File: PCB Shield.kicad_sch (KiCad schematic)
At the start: 48 parts, among them J1 Conn_20to49, J10 TB002-500-02BE, J11 Conn_1to20, J12 TB002-500-02BE, J13 TB002-500-02BE, J14 TB002-500-02BE, J15 TB002-500-02BE, J16 TB002-500-02BE, J17 TB002-500-02BE, J18 TB002-500-02BE, J2 Conn_01x08_Socket, J3 Conn_20to49, J6 Conn_01x04_Socket, J7 Conn_01x04_Socket, J8 Conn_1to20, J9 OSTT7020150, Q1 IRLML2502TRPBF, SW1 C1353VQNAA, U2 74AHCT125S14-13, U3 ESDA6V1L

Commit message: final saves
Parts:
- J1, J3: footprint Connector_PinHeader_2.54mm:PinHeader_1x20_P2.54mm_Vertical -> 196_Project_Footprints:196_Conn_20to48
- J11, J8: footprint Connector_PinHeader_2.54mm:PinHeader_1x20_P2.54mm_Vertical -> 196_Project_Footprints:196_Conn_1to20
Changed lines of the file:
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@@
 			)
 		)
-		(property "Footprint" "Connector_PinHeader_2.54mm:PinHeader_1x20_P2.54mm_Vertical"
+		(property "Footprint" "196_Project_Footprints:196_Conn_1to20"
 			(at 115.57 49.53 0)
 			(hide yes)
@@
 			)
 		)
-		(property "Footprint" "Connector_PinHeader_2.54mm:PinHeader_1x20_P2.54mm_Vertical"
+		(property "Footprint" "196_Project_Footprints:196_Conn_20to48"
 			(at 131.318 22.86 0)
 			(hide yes)
@@
 			)
 		)
-		(property "Footprint" "Connector_PinHeader_2.54mm:PinHeader_1x20_P2.54mm_Vertical"
+		(property "Footprint" "196_Project_Footprints:196_Conn_20to48"
 			(at 122.428 22.86 0)
 			(hide yes)
@@
 			)
 		)
-		(property "Footprint" "Connector_PinHeader_2.54mm:PinHeader_1x20_P2.54mm_Vertical"
+		(property "Footprint" "196_Project_Footprints:196_Conn_1to20"
 			(at 106.68 49.53 0)
 			(hide yes)

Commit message: routing almost done
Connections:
- net 3V3 is gone; now on net +3V3: VR2.1, VR3.1
- net +5V: no longer J6.3 (Pin_3), J7.3 (Pin_3)
- net +5V_Limited: now reaches C1.1, C2.1, J1.5V (Pin_19), J3.5V (Pin_19), SW1.1
- net +5V_Limited: now also J6.3 (Pin_3), J7.3 (Pin_3)

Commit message: routing progress + planning
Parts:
- added R4: 0, Resistor_SMD:R_1206_3216Metric, symbol Device:R_Small_US
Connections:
- net +5V: now also SW1.1, R4.2
- net +5V_Limited renamed +5Vlimited
- net +5Vlimited: now also R4.1; no longer SW1.1
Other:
- moved on the sheet: C1, C2

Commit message: most of routing finished
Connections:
- net +5V: no longer C3.2, D1.2, D3.2, D5.2, D7.2, U2.14 (VCC), U3.2
- net +5Vlimited: now also C3.2, D1.2, D3.2, D5.2, D7.2, U2.14 (VCC), U3.2
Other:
- note added: "connect 2 to NMOS drain"
- note removed: "connect to NMOS drain"

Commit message: finished routing and now just need to check 3d models
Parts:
- added H1, H2, H3, H4: MountingHole, MountingHole:MountingHole_3.2mm_M3_DIN965_Pad_TopBottom, symbol Mechanical:MountingHole
- R4: value 0 -> R_Small_US
- renumbered C6 to C3, C5 to C4, C9 to C5, C7 to C6, C3 to C7, C11 to C8, C10 to C9, J11 to J1, J13 to J10, J12 to J11, J16 to J12, J14 to J13, J15 to J14, J18 to J15, J17 to J16, J8 to J3, J1 to J4, J3 to J5, J9 to J8, J10 to J9, R11 to R1, R1 to R2, R2 to R5, R7 to R6, R6 to R7, R9 to R8, R8 to R9, U3 to U1, VR3 to VR1
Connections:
- net +5V: no longer R3.2, R5.2
- net +5Vlimited: now also R3.2, R5.2

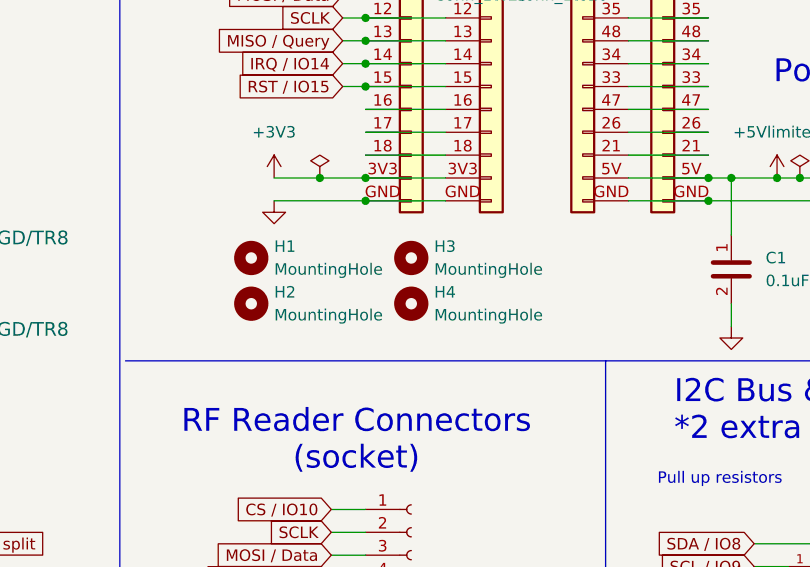
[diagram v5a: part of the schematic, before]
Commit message: updated header pins
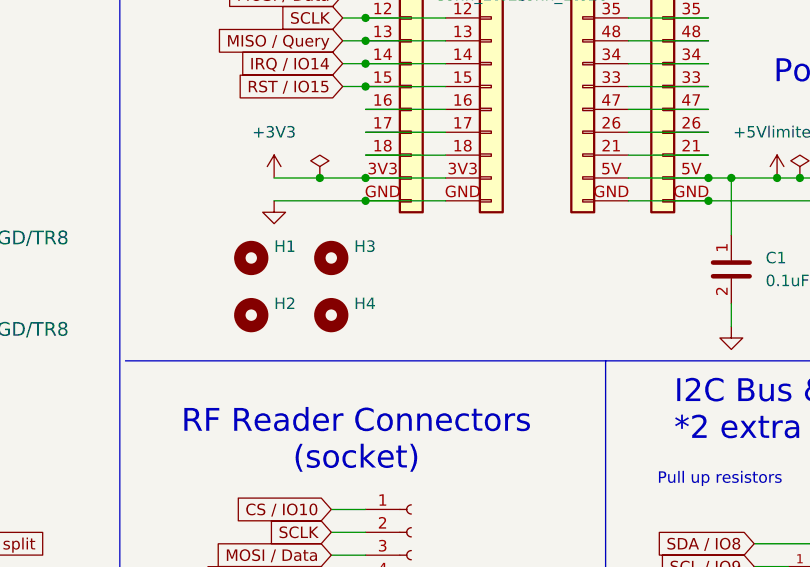
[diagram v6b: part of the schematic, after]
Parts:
- H1, H2, H3, H4: footprint MountingHole:MountingHole_3.2mm_M3_DIN965_Pad_TopBottom -> 196_Project_Footprints:MountingHole_3.2mm_M3_Pad_Via
- J2: footprint Connector_PinSocket_2.54mm:PinSocket_1x08_P2.54mm_Vertical -> 196_Project_Footprints:PinSocket_1x08_P2.54mm_Vertical

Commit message: made shopping list
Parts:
- removed R4: R_Small_US, Resistor_SMD:R_1206_3216Metric, symbol Device:R_Small_US
- added R4: 0, Resistor_SMD:R_1206_3216Metric, symbol 196_Project:RCS12060000Z0EA
- C1, C7: MANUFACTURER (none) -> Aillen; Part Number (none) -> 1206B104K500BD
- C2: MANUFACTURER (none) -> Aillen; Part Number (none) -> 1206B105K250JC
- C3, C4, C5, C6, C8, C9: MANUFACTURER (none) -> Rubycon; Part Number (none) -> 25ZLH470MEFC10X12.5
- D1, D2, D3, D4, D5, D6, D7, D8: MANUFACTURER (none) -> Visual Communications Company - VCC; Part Number (none) -> CMD17-21VGD/TR8
- J1, J3, J4, J5: MANUFACTURER (none) -> Würth Elektronik; Part Number (none) -> 61302011121
- J10, J11, J12, J13, J14, J15, J16, J9: Part Number (none) -> TB002-500-02BE
- J2: MANUFACTURER (none) -> Würth Elektronik; Part Number (none) -> 61300811121
- J6, J7: MANUFACTURER (none) -> Würth Elektronik; Part Number (none) -> 61300411121
- J8: MANUFACTURER (none) -> On Shore Technology Inc.; Part Number (none) -> OSTT7020150
- LS1: Part Number (none) -> AI-3035-TWT-3V-R
- Q1: value IRLML2502TRPBF -> DMN2075U-7; MANUFACTURER (none) -> Diodes Incorporated; Part Number (none) -> DMN2075U-7
- R1, R6, R7, R8, R9: MANUFACTURER (none) -> Stackpole Electronics Inc; Part Number (none) -> RMCF1206FT220R
- R2: MANUFACTURER (none) -> Vishay Dale; Part Number (none) -> CRCW120616R2FKEA
- R3, R5: MANUFACTURER (none) -> YAGEO; Part Number (none) -> RC1206FR-074K7L
- SW1: MANUFACTURER (none) -> Bulgin; Part Number (none) -> C1353VQNAA
- U1: MANUFACTURER (none) -> STMicroelectronics; Part Number (none) -> ESDA6V1L
- U2: MANUFACTURER (none) -> Diodes Incorporated; Part Number (none) -> 74AHCT125S14-13
- VR1, VR2: Part Number (none) -> 3361P-1-103GLF
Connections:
- net +5V: now also R4.2
- net +5Vlimited: now also R4.1
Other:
- moved on the sheet: C1, C2, J6, J7

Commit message: swapped out out of stock / weird order components
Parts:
- C1, C7: MANUFACTURER Aillen -> Samsung Electro-Mechanics; Part Number 1206B104K500BD -> CL31B104KBCNNNC
- C2: MANUFACTURER Aillen -> Samsung Electro-Mechanics; Part Number 1206B105K250JC -> CL31B105KAHNNNE
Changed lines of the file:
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@@
 			)
 		)
-		(property "Part Number" "1206B104K500BD"
+		(property "Part Number" "CL31B104KBCNNNC"
 			(at 267.97 88.9 90)
 			(hide yes)
@@
 			)
 		)
-		(property "MANUFACTURER" "Aillen"
+		(property "MANUFACTURER" "Samsung Electro-Mechanics"
 			(at 267.97 88.9 90)
 			(hide yes)
@@
 			)
 		)
-		(property "Description" "CAP SMD 1206 X7R 1UF 10 25V"
+		(property "Description" "CAP CER 1UF 25V X7R 1206"
 			(at 145.288 100.33 0)
 			(hide yes)
@@
 			)
 		)
-		(property "Part Number" "1206B105K250JC "
+		(property "Part Number" "CL31B105KAHNNNE"
 			(at 143.51 87.63 90)
 			(hide yes)
@@
 			)
 		)
-		(property "MANUFACTURER" "Aillen"
+		(property "MANUFACTURER" "Samsung Electro-Mechanics"
 			(at 143.51 87.63 0)
 			(hide yes)
@@
 			)
 		)
-		(property "Part Number" "1206B104K500BD"
+		(property "Part Number" "CL31B104KBCNNNC"
 			(at 135.89 83.82 90)
 			(hide yes)
@@
 			)
 		)
-		(property "MANUFACTURER" "Aillen"
+		(property "MANUFACTURER" "Samsung Electro-Mechanics"
 			(at 135.89 83.82 0)
 			(hide yes)
